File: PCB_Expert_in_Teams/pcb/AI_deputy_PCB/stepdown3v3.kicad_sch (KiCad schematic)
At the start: 16 parts, among them IC6 LM25576QMH_NOPB

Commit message: 29/10/update
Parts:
- removed C28, C30: 0.01u, symbol Device:C_Polarized_US
- added C28, C30: 0.01u, Capacitor_SMD:C_0805_2012Metric_Pad1.18x1.45mm_HandSolder, symbol Device:C
- added C36, C37: 10u, Capacitor_SMD:C_0805_2012Metric_Pad1.18x1.45mm_HandSolder, symbol Device:C
- added R19: 510, Resistor_SMD:R_0805_2012Metric_Pad1.20x1.40mm_HandSolder, symbol Device:R
- C27: value 3.3u -> 68u
- C29, C31, C32, C34, C35: footprint (none) -> Capacitor_SMD:C_0805_2012Metric_Pad1.18x1.45mm_HandSolder
- D2: footprint DIOM7958X256N -> EXT_AI_DEPUTY_Library:DIOM7958X256N
- L2: value 4.7u -> 8.2u
- R15, R17, R18: footprint (none) -> Resistor_SMD:R_0805_2012Metric_Pad1.20x1.40mm_HandSolder
- R16: value 3.57k -> 10k; footprint (none) -> Resistor_SMD:R_0805_2012Metric_Pad1.20x1.40mm_HandSolder
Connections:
- net GND: now also C30.2, C36.2, C37.2, R19.2; no longer R16.2
- net VIN: now also C36.1, C37.1
- net at IC6.7 (FB), R17.2, R18.1: now also C28.2
- net at IC6.11 (SS): now also C30.1
- net at R15.2: now also C28.1
- new net: R16.2, R19.1
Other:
- note added: "The Diode IS a Schottky Diode although the symbol shows otherwise could choose a diode with lower VRRM for even more efficency (20-30V indstead)"
- note removed: "The Diode IS a Schottky Diode although the symbol shows otherwise"
- moved on the sheet: C27, R16

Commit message: update pcb from desktop
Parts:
- C27: footprint (none) -> EXT_AI_DEPUTY_Library:T520D
- C33: footprint (none) -> EXT_AI_DEPUTY_Library:SX_Package
- IC6: footprint SOP65P640X110-21N -> EXT_AI_DEPUTY_Library:SOP65P640X110-21N
- L2: footprint (none) -> EXT_AI_DEPUTY_Library:INDPM7166X300N
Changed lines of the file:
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@@
-	)
-	(junction
-		(at 208.28 77.47)
-		(diameter 0)
-		(color 0 0 0 0)
 	)
 	(junction
@@
 	(junction
 		(at 168.91 81.28)
+		(diameter 0)
+		(color 0 0 0 0)
+	)
+	(junction
+		(at 208.28 77.47)
 		(diameter 0)
 		(color 0 0 0 0)
@@
 			)
 		)
-		(property "Footprint" ""
+		(property "Footprint" "EXT_AI_DEPUTY_Library:SX_Package"
 			(at 208.28 81.28 0)
 			(effects
@@
 			)
 		)
-		(property "Datasheet" "~"
+		(property "Datasheet" "https://www.farnell.com/datasheets/4379350.pdf"
 			(at 208.28 81.28 0)
 			(effects
@@
 			)
 		)
-		(property "Footprint" ""
+		(property "Footprint" "EXT_AI_DEPUTY_Library:INDPM7166X300N"
 			(at 200.66 77.47 0)
 			(effects
@@
 			)
 		)
-		(property "Datasheet" "~"
+		(property "Datasheet" "https://docs.rs-online.com/542b/A700000008249143.pdf"
 			(at 200.66 77.47 0)
 			(effects
@@
 			)
 		)
-		(property "Footprint" "SOP65P640X110-21N"
+		(property "Footprint" "EXT_AI_DEPUTY_Library:SOP65P640X110-21N"
 			(at 165.1 171.12 0)
 			(effects
@@
 			)
 		)
-		(property "Footprint" ""
+		(property "Footprint" "EXT_AI_DEPUTY_Library:T520D"
 			(at 72.39 87.63 0)
 			(effects
@@
 			)
 		)
-		(property "Datasheet" "~"
+		(property "Datasheet" "https://www.mouser.dk/datasheet/3/508/1/KEM_T2076_T52X_530.pdf"
 			(at 72.39 87.63 0)
 			(effects

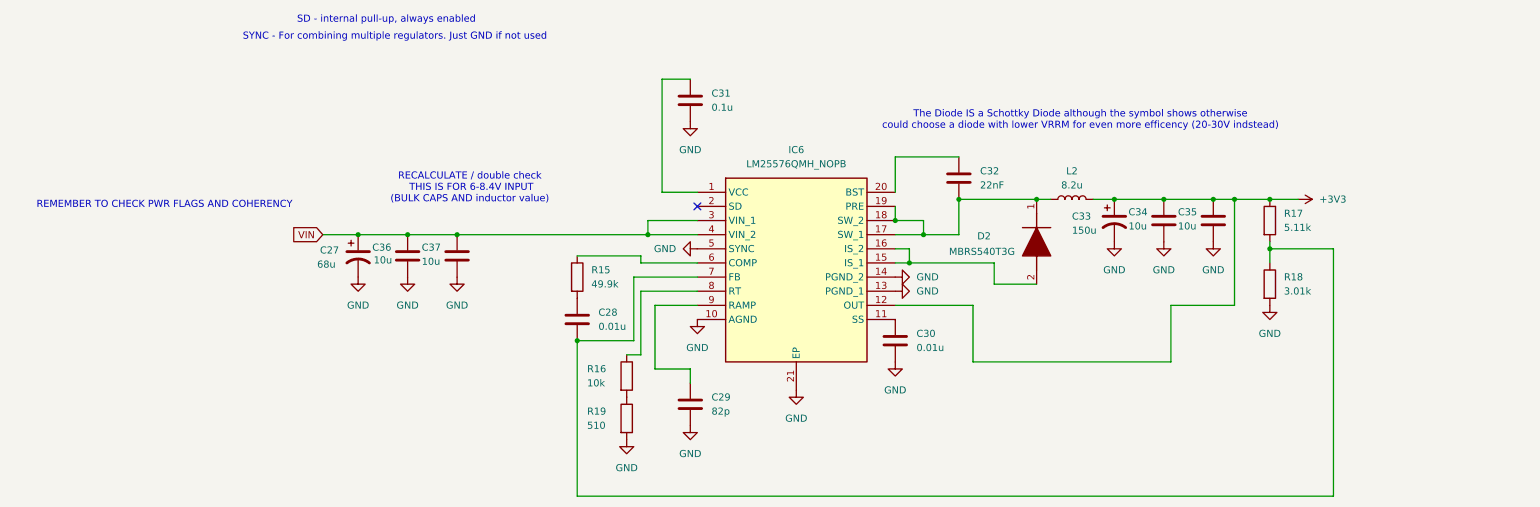
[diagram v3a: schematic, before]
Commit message: pcb updates from desktop with schematic fix
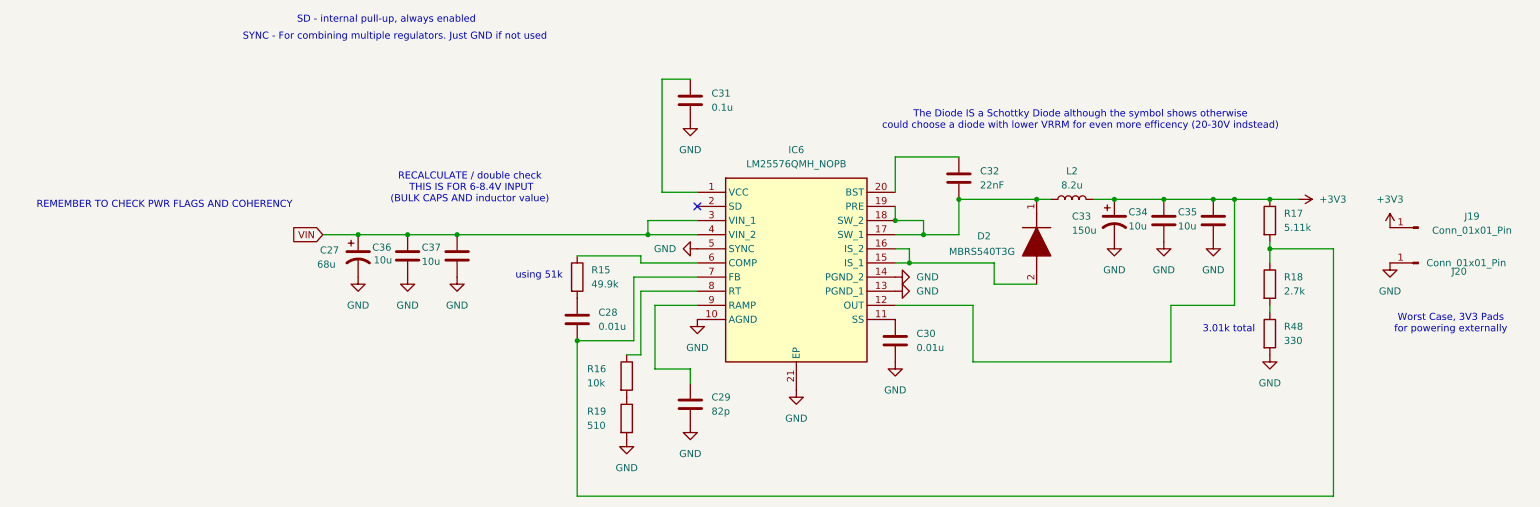
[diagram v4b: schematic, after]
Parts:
- added J19, J20: Conn_01x01_Pin, TestPoint:TestPoint_Pad_4.0x4.0mm, symbol Connector:Conn_01x01_Pin
- added R48: 330, Resistor_SMD:R_0805_2012Metric_Pad1.20x1.40mm_HandSolder, symbol Device:R
- R18: value 3.01k -> 2.7k
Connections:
- net +3V3: now also J19.1 (Pin_1)
- net GND: now also J20.1 (Pin_1), R48.2; no longer R18.2
- new net: R18.2, R48.1
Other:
- note added: "3.01k total"
- note added: "Worst Case, 3V3 Pads for powering externally"
- note added: "using 51k"

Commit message: update after lab session with gustav saturday
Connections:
- net VIN renamed +BATT
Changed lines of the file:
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@@
-		)
-	)
-	(global_label "VIN"
-		(shape input)
-		(at 66.04 83.82 180)
-		(fields_autoplaced yes)
-		(effects
-			(font
-				(size 1.27 1.27)
-			)
-			(justify right)
-		)
-		(property "Intersheetrefs" "${INTERSHEET_REFS}"
-			(at 60.0309 83.82 0)
-			(effects
-				(font
-					(size 1.27 1.27)
-				)
-				(justify right)
-				(hide yes)
-			)
 		)
 	)
@@
 					(unit 1)
 				)
+			)
+		)
+	)
+	(symbol
+		(lib_id "power:+BATT")
+		(at 66.04 83.82 90)
+		(unit 1)
+		(exclude_from_sim no)
+		(in_bom yes)
+		(on_board yes)
+		(dnp no)
+		(fields_autoplaced yes)
+		(property "Reference" "#PWR0127"
+			(at 69.85 83.82 0)
+			(effects
+				(font
+					(size 1.27 1.27)
+				)
+				(hide yes)
+			)
+		)
+		(property "Value" "+BATT"
+			(at 62.23 83.8199 90)
+			(effects
+				(font
+					(size 1.27 1.27)
+				)
+				(justify left)
+			)
+		)
+		(property "Footprint" ""
+			(at 66.04 83.82 0)
+			(effects
+				(font
+					(size 1.27 1.27)
+				)
+				(hide yes)
+			)
+		)
+		(property "Datasheet" ""
+			(at 66.04 83.82 0)
+			(effects
+				(font
+					(size 1.27 1.27)
+				)
+				(hide yes)
+			)
+		)
+		(property "Description" "Power symbol creates a global label with name \"+BATT\""
+			(at 66.04 83.82 0)
+			(effects
+				(font
+					(size 1.27 1.27)
+				)
+				(hide yes)
+			)
+		)
+		(pin "1"
+		)
+		(instances
+			(project ""
+				(path "/3784b751-4d5b-4452-8288-14e483e1cb48/82ecce59-750a-4f55-a6e5-60f0e896ad8e"
+					(reference "#PWR0127")
+					(unit 1)
+				)

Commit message: finished PCB design and gerbers are in directory
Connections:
- net +BATT renamed +VDC
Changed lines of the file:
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@@
 	(wire
 		(pts
-			(xy 66.04 83.82) (xy 72.39 83.82)
+			(xy 64.77 83.82) (xy 72.39 83.82)
 		)
 		(stroke
@@
 	)
 	(symbol
-		(lib_id "power:+BATT")
-		(at 66.04 83.82 90)
-		(unit 1)
-		(exclude_from_sim no)
-		(in_bom yes)
-		(on_board yes)
-		(dnp no)
-		(fields_autoplaced yes)
-		(property "Reference" "#PWR0127"
-			(at 69.85 83.82 0)
-			(effects
-				(font
-					(size 1.27 1.27)
-				)
-				(hide yes)
-			)
-		)
-		(property "Value" "+BATT"
-			(at 62.23 83.8199 90)
-			(effects
-				(font
-					(size 1.27 1.27)
-				)
-				(justify left)
-			)
-		)
-		(property "Footprint" ""
-			(at 66.04 83.82 0)
-			(effects
-				(font
-					(size 1.27 1.27)
-				)
-				(hide yes)
-			)
-		)
-		(property "Datasheet" ""
-			(at 66.04 83.82 0)
-			(effects
-				(font
-					(size 1.27 1.27)
-				)
-				(hide yes)
-			)
-		)
-		(property "Description" "Power symbol creates a global label with name \"+BATT\""
-			(at 66.04 83.82 0)
-			(effects
-				(font
-					(size 1.27 1.27)
-				)
-				(hide yes)
-			)
-		)
-		(pin "1"
-		)
-		(instances
-			(project ""
-				(path "/3784b751-4d5b-4452-8288-14e483e1cb48/82ecce59-750a-4f55-a6e5-60f0e896ad8e"
-					(reference "#PWR0127")
-					(unit 1)
-				)
-			)
-		)
-	)
-	(symbol
 		(lib_id "power:GND")
 		(at 133.35 86.36 270)
@@
 					(unit 1)
 				)
+			)
+		)
+	)
+	(symbol
+		(lib_id "power:+VDC")
+		(at 64.77 83.82 90)
+		(unit 1)
+		(exclude_from_sim no)
+		(in_bom yes)
+		(on_board yes)
+		(dnp no)
+		(fields_autoplaced yes)
+		(property "Reference" "#PWR0127"
+			(at 67.31 83.82 0)
+			(effects
+				(font
+					(size 1.27 1.27)
+				)
+				(hide yes)
+			)
+		)
+		(property "Value" "+VDC"
+			(at 58.42 83.8199 90)
+			(effects
+				(font
+					(size 1.27 1.27)
+				)
+				(justify left)
+			)
+		)
+		(property "Footprint" ""
+			(at 64.77 83.82 0)
+			(effects
+				(font
+					(size 1.27 1.27)
+				)
+				(hide yes)
+			)
+		)
+		(property "Datasheet" ""
+			(at 64.77 83.82 0)
+			(effects
+				(font
+					(size 1.27 1.27)
+				)
+				(hide yes)
+			)
+		)
+		(property "Description" "Power symbol creates a global label with name \"+VDC\""
+			(at 64.77 83.82 0)
+			(effects
+				(font
+					(size 1.27 1.27)
+				)
+				(hide yes)
+			)
+		)
+		(pin "1"
+		)
+		(instances
+			(project "AI_deputy_PCB"
+				(path "/3784b751-4d5b-4452-8288-14e483e1cb48/82ecce59-750a-4f55-a6e5-60f0e896ad8e"
+					(reference "#PWR0127")
+					(unit 1)
+				)

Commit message: updated pcb code
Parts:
- R15: value 49.9k -> 51k
- R17: value 5.11k -> 5.1k
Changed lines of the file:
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@@
 			)
 		)
-		(property "Value" "5.11k"
+		(property "Value" "5.1k"
 			(at 238.76 82.5499 0)
 			(effects
@@
 			)
 		)
-		(property "Value" "49.9k"
+		(property "Value" "51k"
 			(at 114.3 92.7099 0)
 			(effects
